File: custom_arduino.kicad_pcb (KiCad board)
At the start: 2 copper layers, 69.3 x 63 mm, 47 parts, among them J1 USB_B_Mini, J10 Conn_01x10, J2 Barrel_Jack, J3 Conn_01x08, J4 Conn_01x08, J5 Conn_01x06, J6 Conn_01x06, J7 Conn_01x08, J8 Conn_01x08, J9 Conn_01x10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

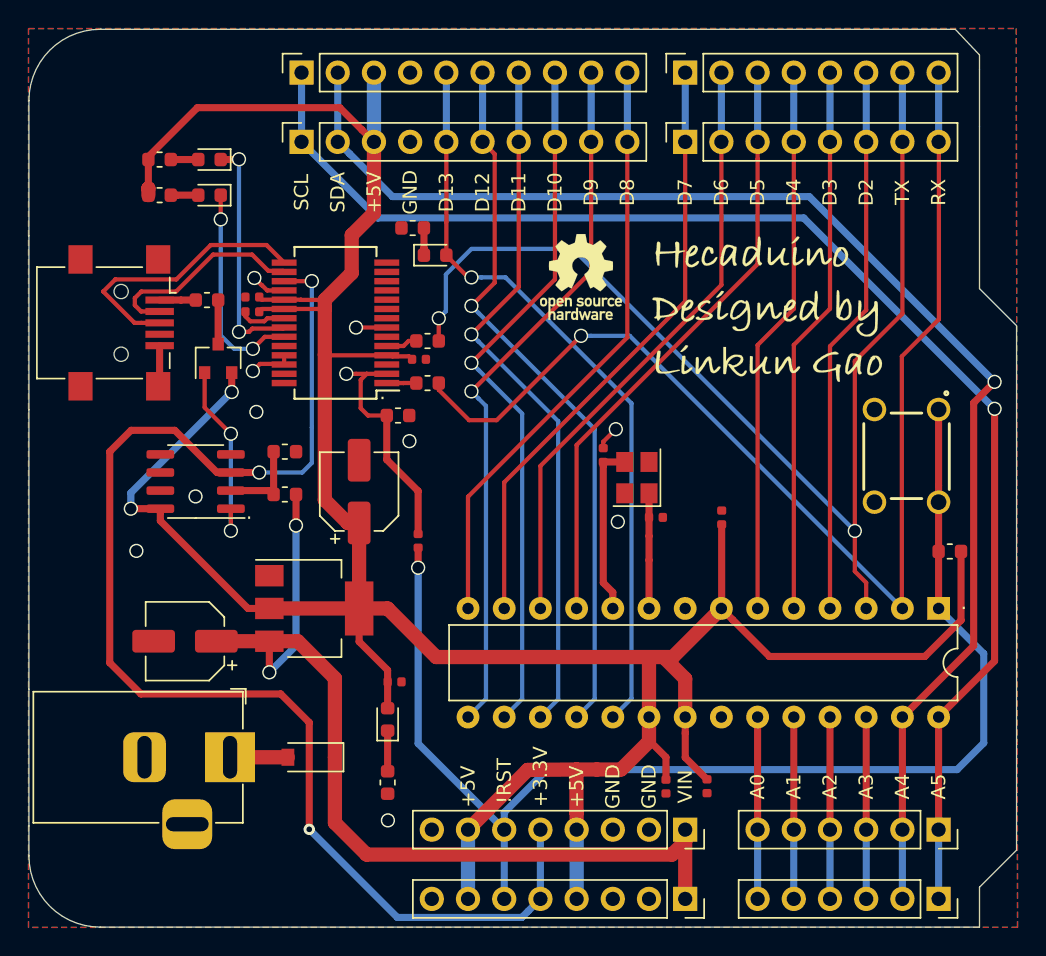
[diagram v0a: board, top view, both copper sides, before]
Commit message: Round a corner and move a capacitor away from DC jack
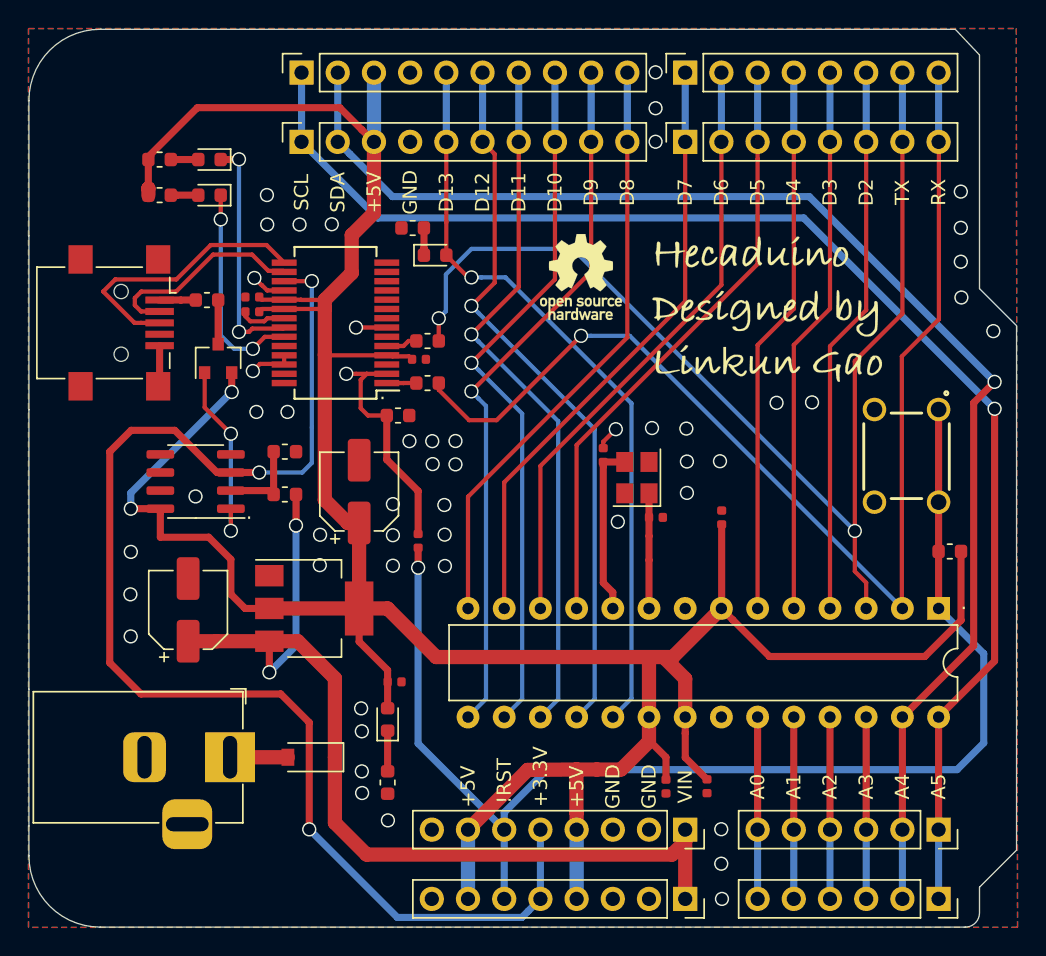
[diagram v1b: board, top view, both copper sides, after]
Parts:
- moved C4 2.21 mm to (90.0, 94.1), turned to 90 degrees
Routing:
- net +5V: track 224.9 -> 227.0 mm
- net VIN: track 66.6 -> 68.5 mm
- net GND: vias 10 -> 51
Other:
- outline, holes or cut-outs redrawn
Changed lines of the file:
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@@
   (general
     (thickness 1.6)
-    (drawings 53)
-    (tracks 386)
+    (drawings 54)
+    (tracks 431)
     (zones 0)
     (modules 47)
@@
   )
   (module Capacitor_SMD:CP_Elec_5x5.4 (layer F.Cu)
-    (at 89.78 96.3 180)
+    (at 90 94.1 90)
     (descr "SMD capacitor, aluminum electrolytic, Nichicon, 5.0x5.4mm")
     (tags "capacitor electrolytic")
     (attr smd)
-    (fp_text reference C4 (at 0 -3.7) (layer F.Fab)
+    (fp_text reference C4 (at 0 -3.7 90) (layer F.Fab)
       (effects (font (size 1 1) (thickness 0.15)))
     )
-    (fp_text value 47uF (at 0 3.7) (layer F.Fab)
+    (fp_text value 47uF (at 0 3.7 90) (layer F.Fab)
       (effects (font (size 1 1) (thickness 0.15)))
     )
-    (fp_text user %R (at 0 0) (layer F.Fab)
+    (fp_text user %R (at 0 0 90) (layer F.Fab)
       (effects (font (size 1 1) (thickness 0.15)))
     )
@@
     (fp_line (start 2.65 -2.65) (end 2.65 2.65) (layer F.Fab) (width 0.1))
     (fp_circle (center 0 0) (end 2.5 0) (layer F.Fab) (width 0.1))
-    (pad 2 smd roundrect (at 2.2 0 180) (size 3 1.6) (layers F.Cu F.Paste F.Mask) (roundrect_rratio 0.15625)
+    (pad 2 smd roundrect (at 2.2 0 90) (size 3 1.6) (layers F.Cu F.Paste F.Mask) (roundrect_rratio 0.15625)
       (net 1 GND))
-    (pad 1 smd roundrect (at -2.2 0 180) (size 3 1.6) (layers F.Cu F.Paste F.Mask) (roundrect_rratio 0.15625)
+    (pad 1 smd roundrect (at -2.2 0 90) (size 3 1.6) (layers F.Cu F.Paste F.Mask) (roundrect_rratio 0.15625)
       (net 3 VIN))
     (model ${KISYS3DMOD}/Capacitor_SMD.3dshapes/CP_Elec_5x5.4.wrl
@@
     )
   )
+  (gr_arc (start 144.53 115.36) (end 144.53 116.36) (angle -90) (layer Edge.Cuts) (width 0.05))
   (gr_text SDA (at 100.5 64.8 90) (layer F.SilkS)
     (effects (font (size 1 1) (thickness 0.15)))
@@
   (gr_line (start 148.13 106.96) (end 148.13 74.16) (layer Edge.Cuts) (width 0.05))
   (gr_line (start 145.53 113.56) (end 148.13 110.96) (layer Edge.Cuts) (width 0.05))
-  (gr_line (start 145.53 116.36) (end 145.53 113.56) (layer Edge.Cuts) (width 0.05))
-  (gr_line (start 83.83 116.36) (end 145.53 116.36) (layer Edge.Cuts) (width 0.05))
+  (gr_line (start 145.53 115.36) (end 145.53 113.56) (layer Edge.Cuts) (width 0.05))
+  (gr_line (start 83.83 116.36) (end 144.53 116.36) (layer Edge.Cuts) (width 0.05))
   (via (at 120.15 87.92) (size 1) (drill 0.8) (layers F.Cu B.Cu) (net 1))
   (via (at 94.79 80.21) (size 1) (drill 0.8) (layers F.Cu B.Cu) (net 1))
-  (via (at 86.37 89.96) (size 1) (drill 0.8) (layers F.Cu B.Cu) (net 1))
+  (via (at 85.98 90.03) (size 1) (drill 0.8) (layers F.Cu B.Cu) (net 1))
   (via (at 90.52 86.14) (size 1) (drill 0.8) (layers F.Cu B.Cu) (net 1))
   (via (at 104.02 108.87) (size 1) (drill 0.8) (layers F.Cu B.Cu) (net 1))
@@
   (segment (start 88 75.56) (end 88 78.31) (width 0.5) (layer F.Cu) (net 1))
   (segment (start 88 78.31) (end 87.9 78.41) (width 0.5) (layer F.Cu) (net 1))
+  (via (at 107.13 82.26) (size 1) (drill 0.8) (layers F.Cu B.Cu) (net 1))
+  (via (at 108.76 82.25) (size 1) (drill 0.8) (layers F.Cu B.Cu) (net 1))
+  (via (at 107.16 83.87) (size 1) (drill 0.8) (layers F.Cu B.Cu) (net 1))
+  (via (at 108.76 83.89) (size 1) (drill 0.8) (layers F.Cu B.Cu) (net 1))
+  (via (at 95.53 64.99) (size 1) (drill 0.8) (layers F.Cu B.Cu) (net 1))
+  (via (at 95.55 67.06) (size 1) (drill 0.8) (layers F.Cu B.Cu) (net 1))
+  (via (at 97.82 67.06) (size 1) (drill 0.8) (layers F.Cu B.Cu) (net 1))
+  (via (at 100.08 67.04) (size 1) (drill 0.8) (layers F.Cu B.Cu) (net 1))
+  (via (at 125 83.69) (size 1) (drill 0.8) (layers F.Cu B.Cu) (net 1))
+  (via (at 127.32 83.67) (size 1) (drill 0.8) (layers F.Cu B.Cu) (net 1))
+  (via (at 125 85.89) (size 1) (drill 0.8) (layers F.Cu B.Cu) (net 1))
+  (via (at 124.96 81.38) (size 1) (drill 0.8) (layers F.Cu B.Cu) (net 1))
+  (via (at 122.55 81.34) (size 1) (drill 0.8) (layers F.Cu B.Cu) (net 1))
+  (via (at 131.29 79.57) (size 1) (drill 0.8) (layers F.Cu B.Cu) (net 1))
+  (via (at 133.78 79.54) (size 1) (drill 0.8) (layers F.Cu B.Cu) (net 1))
+  (via (at 144.22 64.75) (size 1) (drill 0.8) (layers F.Cu B.Cu) (net 1))
+  (via (at 144.22 67.29) (size 1) (drill 0.8) (layers F.Cu B.Cu) (net 1))
+  (via (at 144.22 69.67) (size 1) (drill 0.8) (layers F.Cu B.Cu) (net 1))
+  (via (at 144.26 72.18) (size 1) (drill 0.8) (layers F.Cu B.Cu) (net 1))
+  (via (at 146.5 74.54) (size 1) (drill 0.8) (layers F.Cu B.Cu) (net 1))
+  (via (at 85.97 95.96) (size 1) (drill 0.8) (layers F.Cu B.Cu) (net 1))
+  (via (at 85.95 93.01) (size 1) (drill 0.8) (layers F.Cu B.Cu) (net 1))
+  (via (at 107.98 86.74) (size 1) (drill 0.8) (layers F.Cu B.Cu) (net 1))
+  (via (at 108 88.82) (size 1) (drill 0.8) (layers F.Cu B.Cu) (net 1))
+  (via (at 108.02 91.02) (size 1) (drill 0.8) (layers F.Cu B.Cu) (net 1))
+  (via (at 104.37 86.68) (size 1) (drill 0.8) (layers F.Cu B.Cu) (net 1))
+  (via (at 104.37 88.86) (size 1) (drill 0.8) (layers F.Cu B.Cu) (net 1))
+  (via (at 104.37 91) (size 1) (drill 0.8) (layers F.Cu B.Cu) (net 1))
+  (via (at 99.26 88.83) (size 1) (drill 0.8) (layers F.Cu B.Cu) (net 1))
+  (via (at 99.24 90.96) (size 1) (drill 0.8) (layers F.Cu B.Cu) (net 1))
+  (via (at 102.14 101.01) (size 1) (drill 0.8) (layers F.Cu B.Cu) (net 1))
+  (via (at 102.19 102.62) (size 1) (drill 0.8) (layers F.Cu B.Cu) (net 1))
+  (via (at 102.19 105.43) (size 1) (drill 0.8) (layers F.Cu B.Cu) (net 1))
+  (via (at 102.21 106.95) (size 1) (drill 0.8) (layers F.Cu B.Cu) (net 1))
+  (via (at 127.41 109.49) (size 1) (drill 0.8) (layers F.Cu B.Cu) (net 1))
+  (via (at 127.46 114.38) (size 1) (drill 0.8) (layers F.Cu B.Cu) (net 1))
+  (via (at 127.41 111.91) (size 1) (drill 0.8) (layers F.Cu B.Cu) (net 1))
+  (via (at 122.8 56.38) (size 1) (drill 0.8) (layers F.Cu B.Cu) (net 1))
+  (via (at 122.8 61.25) (size 1) (drill 0.8) (layers F.Cu B.Cu) (net 1))
+  (via (at 122.8 58.9) (size 1) (drill 0.8) (layers F.Cu B.Cu) (net 1))
+  (via (at 96.97 80.21) (size 1) (drill 0.8) (layers F.Cu B.Cu) (net 1))
   (via (at 85.98 87) (size 1) (drill 0.8) (layers F.Cu B.Cu) (net 2))
   (via (at 93.06 78.81) (size 1) (drill 0.8) (layers F.Cu B.Cu) (net 2))
@@
   (segment (start 124.88 101.62) (end 124.88 98.93) (width 1) (layer F.Cu) (net 2))
   (segment (start 124.88 98.93) (end 123.36 97.41) (width 1) (layer F.Cu) (net 2))
-  (segment (start 88.05 87.85) (end 88.05 87.3) (width 0.5) (layer F.Cu) (net 2))
-  (segment (start 95.7 94) (end 94.2 94) (width 0.5) (layer F.Cu) (net 2))
-  (segment (start 94.2 94) (end 88.05 87.85) (width 0.5) (layer F.Cu) (net 2))
-  (segment (start 88.05 87.3) (end 88.05 87) (width 0.5) (layer F.Cu) (net 2))
   (segment (start 124.01 97.41) (end 123.36 97.41) (width 1) (layer F.Cu) (net 2))
   (segment (start 127.42 94) (end 124.01 97.41) (width 1) (layer F.Cu) (net 2))
@@
   (segment (start 122.34 101.62) (end 122.34 103.25) (width 0.5) (layer F.Cu) (net 2))
   (segment (start 122.34 103.25) (end 123.53 104.44) (width 0.5) (layer F.Cu) (net 2))
+  (segment (start 88.05 89) (end 88.05 87.3) (width 0.5) (layer F.Cu) (net 2))
+  (segment (start 95.7 94) (end 94 94) (width 0.5) (layer F.Cu) (net 2))
+  (segment (start 94 94) (end 93 93) (width 0.5) (layer F.Cu) (net 2))
+  (segment (start 93 93) (end 93 90.555017) (width 0.5) (layer F.Cu) (net 2))
+  (segment (start 88.05 87.3) (end 88.05 87) (width 0.5) (layer F.Cu) (net 2))
+  (segment (start 93 90.555017) (end 91.444983 89) (width 0.5) (layer F.Cu) (net 2))
+  (segment (start 91.444983 89) (end 88.05 89) (width 0.5) (layer F.Cu) (net 2))
   (via (at 97.57 88.18) (size 1) (drill 0.8) (layers F.Cu B.Cu) (net 3))
   (via (at 95.7 98.48) (size 1) (drill 0.8) (layers F.Cu B.Cu) (net 3))
@@
   (segment (start 97.575 86) (end 97.575 88.175) (width 0.5) (layer F.Cu) (net 3))
   (segment (start 124.88 114.38) (end 124.88 109.52) (width 1) (layer F.Cu) (net 3))
+  (segment (start 91.98 96.3) (end 90 96.3) (width 1) (layer F.Cu) (net 3))
   (via (at 101.1 77.535) (size 1) (drill 0.8) (layers F.Cu B.Cu) (net 4))
   (segment (start 102.11 79.95) (end 102.62 80.46) (width 0.3) (layer F.Cu) (net 4))
@@
   (segment (start 98.5 102) (end 98.5 109.5) (width 0.5) (layer F.Cu) (net 22))
   (segment (start 98.5 109.5) (end 98.5 109.5) (width 0.5) (layer F.Cu) (net 22))
-  (via (at 98.5 109.5) (size 0.8) (drill 0.4) (layers F.Cu B.Cu) (net 22))
+  (via (at 98.5 109.5) (size 1) (drill 0.8) (layers F.Cu B.Cu) (net 22) (status 1000000))
   (segment (start 98.5 109.5) (end 98.51 109.5) (width 0.5) (layer B.Cu) (net 22))
   (segment (start 98.675 71.035) (end 98.68 71.03) (width 0.3) (layer F.Cu) (net 22))
